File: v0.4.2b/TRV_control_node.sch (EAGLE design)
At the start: 47 parts, among them J3 AMP FCI 10103594-0001LF, J4 455-1750-1-ND, J6 AMP FCI 10103594-0001LF, SW1 EVQQ, SW2 EVQQ, U1 PCA9306, U11 915MHz, U2 FT231XQ-R, U5 ATMEGA328P-MU, U8 MCP1703/3.3V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

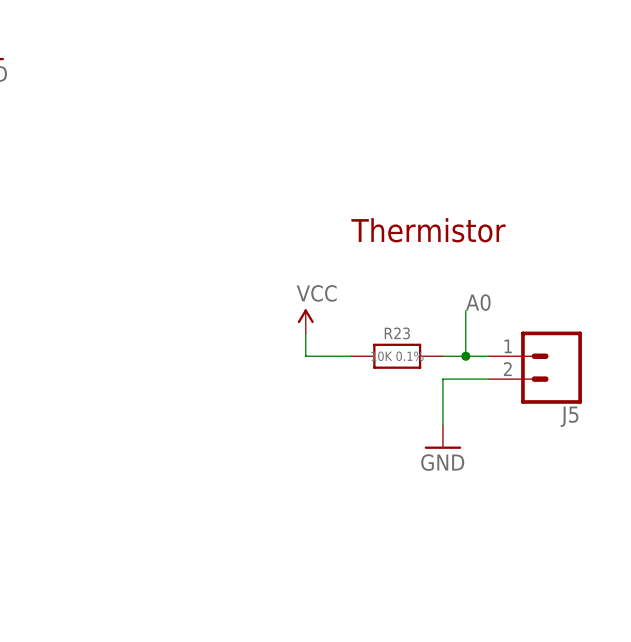
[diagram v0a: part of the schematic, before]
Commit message: v0.4.2b & v0.4.3 - proper versioning & update
- Renamed v0.4.3 to v0.4.2b -- this design is not used as some parts are physically "moved" on the board.
- v0.4.3 - this design now incorporates the following:
- thermistor header pins for extra temperature monitoring if needed
- Relocation of antenna hole away from buttons
- Added SMD pads for servo
- silkscreen update
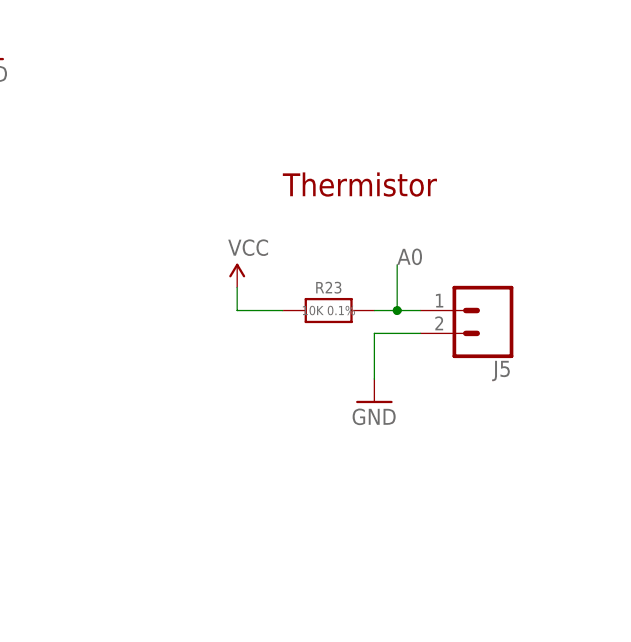
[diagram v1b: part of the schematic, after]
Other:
- moved on the sheet: J5, R23
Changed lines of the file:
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@@
 <text x="99.06" y="35.56" size="2.54" layer="94" font="vector">OLED screen</text>
 <text x="48.26" y="99.06" size="2.54" layer="94" font="vector">Buttons</text>
-<text x="284.48" y="71.12" size="2.54" layer="94" font="vector">Thermistor</text>
+<text x="276.86" y="76.2" size="2.54" layer="94" font="vector">Thermistor</text>
 </plain>
 <instances>
@@
 </instance>
 <instance part="U4" gate="G$1" x="40.64" y="-66.04"/>
-<instance part="SUPPLY5" gate="G$1" x="279.4" y="60.96"/>
-<instance part="J5" gate="G$1" x="307.34" y="58.42" rot="R180"/>
-<instance part="R23" gate="G$1" x="289.56" y="58.42">
-<attribute name="MPN" x="289.56" y="58.42" size="1.778" layer="96" display="off"/>
-</instance>
-<instance part="GND4" gate="1" x="294.64" y="48.26"/>
+<instance part="SUPPLY5" gate="G$1" x="271.78" y="66.04"/>
+<instance part="J5" gate="G$1" x="299.72" y="63.5" rot="R180"/>
+<instance part="R23" gate="G$1" x="281.94" y="63.5">
+<attribute name="MPN" x="281.94" y="63.5" size="1.778" layer="96" display="off"/>
+</instance>
+<instance part="GND4" gate="1" x="287.02" y="53.34"/>
 </instances>
 <busses>
@@
 </segment>
 <segment>
-<wire x1="299.72" y1="55.88" x2="294.64" y2="55.88" width="0.1524" layer="91"/>
-<wire x1="294.64" y1="55.88" x2="294.64" y2="50.8" width="0.1524" layer="91"/>
+<wire x1="292.1" y1="60.96" x2="287.02" y2="60.96" width="0.1524" layer="91"/>
+<wire x1="287.02" y1="60.96" x2="287.02" y2="55.88" width="0.1524" layer="91"/>
 <pinref part="J5" gate="G$1" pin="2"/>
 <pinref part="GND4" gate="1" pin="GND"/>
@@
 <segment>
 <pinref part="SUPPLY5" gate="G$1" pin="VCC"/>
-<wire x1="284.48" y1="58.42" x2="279.4" y2="58.42" width="0.1524" layer="91"/>
-<wire x1="279.4" y1="58.42" x2="279.4" y2="60.96" width="0.1524" layer="91"/>
+<wire x1="276.86" y1="63.5" x2="271.78" y2="63.5" width="0.1524" layer="91"/>
+<wire x1="271.78" y1="63.5" x2="271.78" y2="66.04" width="0.1524" layer="91"/>
 <pinref part="R23" gate="G$1" pin="1"/>
 </segment>
@@
 <net name="A0" class="0">
 <segment>
-<wire x1="299.72" y1="58.42" x2="297.18" y2="58.42" width="0.1524" layer="91"/>
-<wire x1="297.18" y1="58.42" x2="294.64" y2="58.42" width="0.1524" layer="91"/>
-<wire x1="297.18" y1="58.42" x2="297.18" y2="63.5" width="0.1524" layer="91"/>
-<junction x="297.18" y="58.42"/>
-<pinref part="J5" gate="G$1" pin="1"/>
-<pinref part="R23" gate="G$1" pin="2"/>
-<label x="297.18" y="63.5" size="1.778" layer="95"/>
-</segment>
-<segment>
 <pinref part="U5" gate="G$1" pin="PC0"/>
 <wire x1="213.36" y1="144.78" x2="218.44" y2="144.78" width="0.1524" layer="91"/>
 <label x="218.44" y="144.78" size="1.778" layer="95"/>
 </segment>
-</net>
+<segment>
+<wire x1="292.1" y1="63.5" x2="289.56" y2="63.5" width="0.1524" layer="91"/>
+<wire x1="289.56" y1="63.5" x2="287.02" y2="63.5" width="0.1524" layer="91"/>
+<wire x1="289.56" y1="63.5" x2="289.56" y2="68.58" width="0.1524" layer="91"/>
+<junction x="289.56" y="63.5"/>
+<pinref part="J5" gate="G$1" pin="1"/>
+<pinref part="R23" gate="G$1" pin="2"/>
+<label x="289.56" y="68.58" size="1.778" layer="95"/>
+</segment>
+</net>
